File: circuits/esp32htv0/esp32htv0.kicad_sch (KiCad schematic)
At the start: 23 parts, among them J1 Power, SW1 SW_Push, U1 BME280, U2 ESP32-WROOM-32UE, U3 LD1117S33TR_SOT223

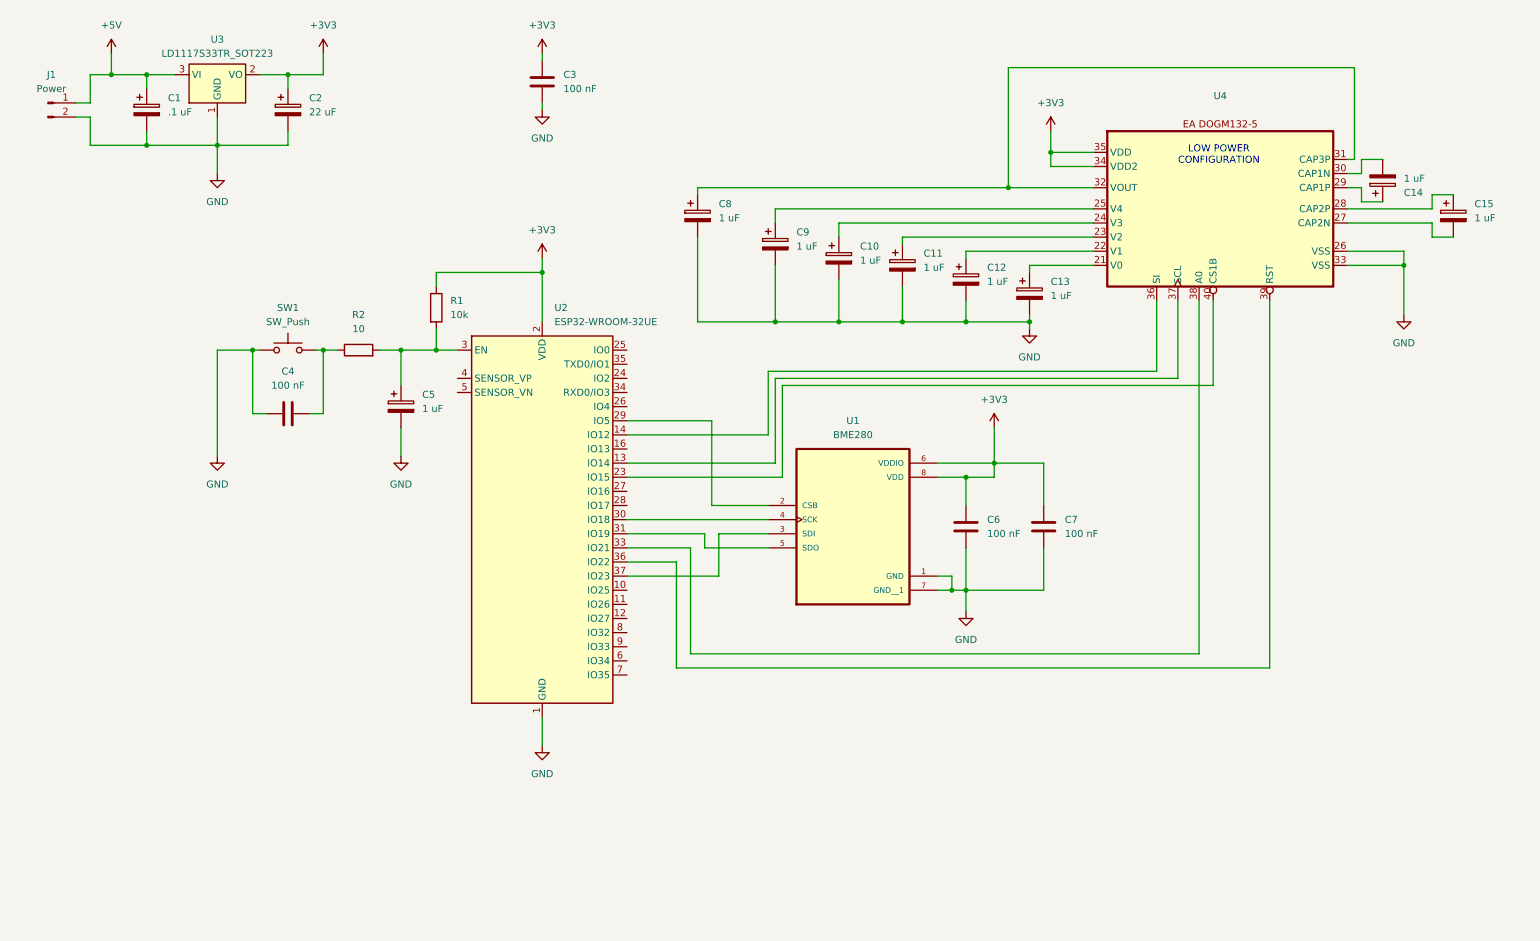
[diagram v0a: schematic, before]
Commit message: Updated ESP32 HTV circuit and a prototype version (esp32htv0) of the same circuit
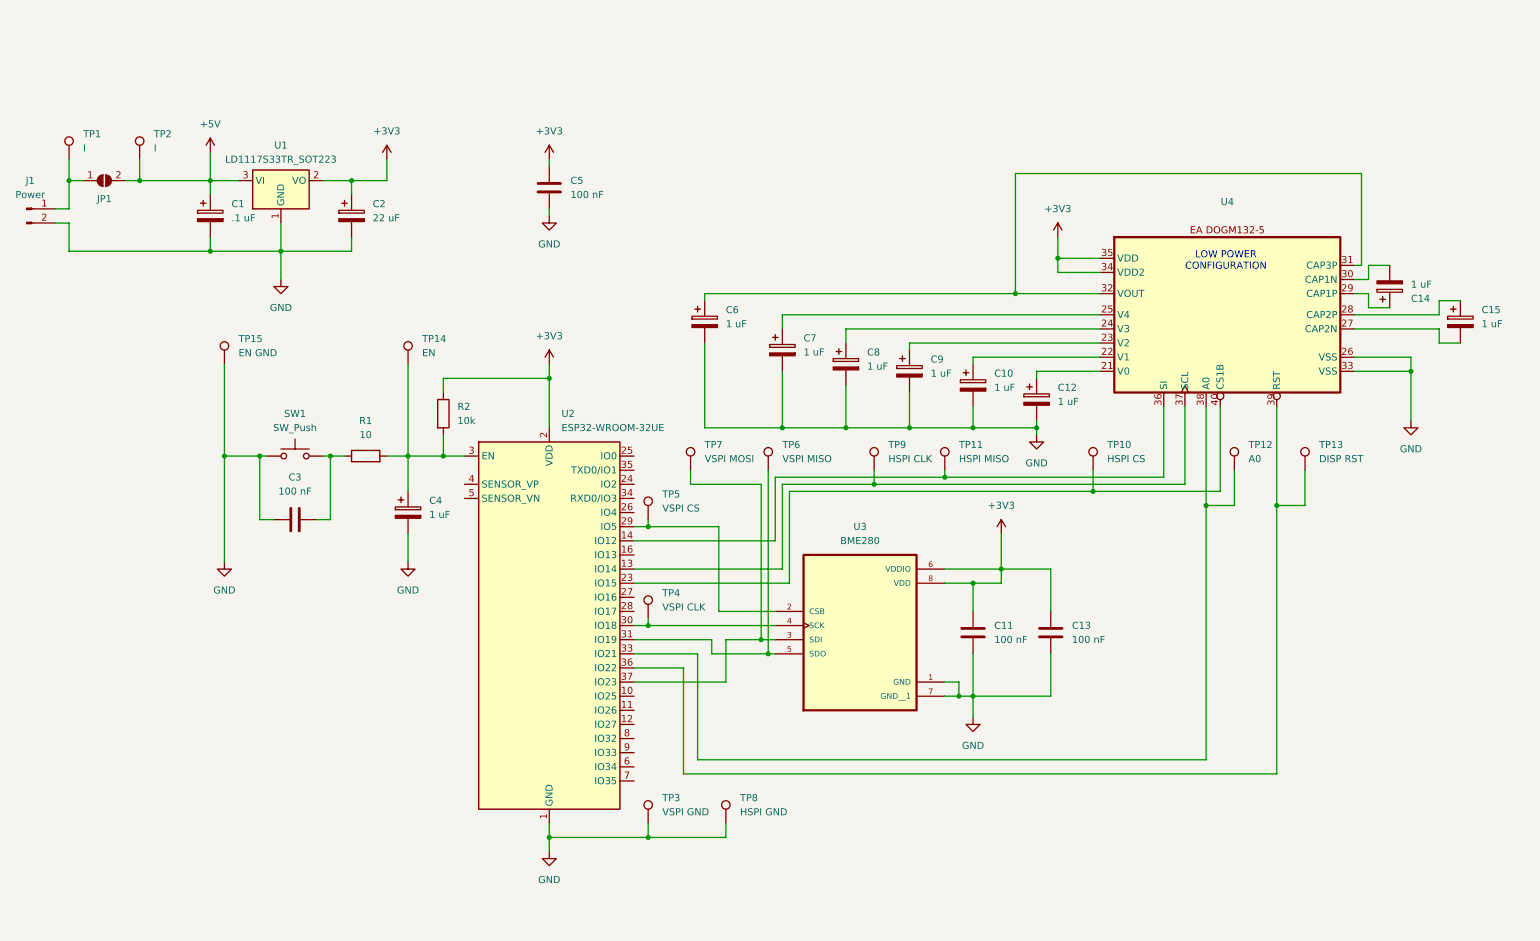
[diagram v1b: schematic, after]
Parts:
- removed C11, C13, C5: 1 uF, Capacitor_SMD:C_1206_3216Metric_Pad1.33x1.80mm_HandSolder, symbol Device:C_Polarized
- removed C4, C6, C7: 100 nF, Capacitor_SMD:C_1206_3216Metric_Pad1.33x1.80mm_HandSolder, symbol Device:C
- removed U1: BME280, gos:PSON65P250X250X100-8N, symbol gos:BME280
- removed U3: LD1117S33TR_SOT223, Package_TO_SOT_SMD:SOT-223-3_TabPin2, symbol Regulator_Linear:LD1117S33TR_SOT223
- added C11, C13, C5: 100 nF, Capacitor_SMD:C_1206_3216Metric_Pad1.33x1.80mm_HandSolder, symbol Device:C
- added C4, C6, C7: 1 uF, Capacitor_SMD:C_1206_3216Metric_Pad1.33x1.80mm_HandSolder, symbol Device:C_Polarized
- added JP1: ID_WP, Jumper:SolderJumper-2_P1.3mm_Open_RoundedPad1.0x1.5mm, symbol Jumper:SolderJumper_2_Open
- added TP1, TP2: I, TestPoint:TestPoint_Loop_D2.50mm_Drill1.0mm, symbol Connector:TestPoint
- added TP10: HSPI CS, TestPoint:TestPoint_Loop_D2.50mm_Drill1.0mm, symbol Connector:TestPoint
- added TP11: HSPI MISO, TestPoint:TestPoint_Loop_D2.50mm_Drill1.0mm, symbol Connector:TestPoint
- added TP12: A0, TestPoint:TestPoint_Loop_D2.50mm_Drill1.0mm, symbol Connector:TestPoint
- added TP13: DISP RST, TestPoint:TestPoint_Loop_D2.50mm_Drill1.0mm, symbol Connector:TestPoint
- added TP14: EN, TestPoint:TestPoint_Loop_D2.50mm_Drill1.0mm, symbol Connector:TestPoint
- added TP15: EN GND, TestPoint:TestPoint_Loop_D2.50mm_Drill1.0mm, symbol Connector:TestPoint
- added TP3: VSPI GND, TestPoint:TestPoint_Loop_D2.50mm_Drill1.0mm, symbol Connector:TestPoint
- added TP4: VSPI CLK, TestPoint:TestPoint_Loop_D2.50mm_Drill1.0mm, symbol Connector:TestPoint
- added TP5: VSPI CS, TestPoint:TestPoint_Loop_D2.50mm_Drill1.0mm, symbol Connector:TestPoint
- added TP6: VSPI MISO, TestPoint:TestPoint_Loop_D2.50mm_Drill1.0mm, symbol Connector:TestPoint
- added TP7: VSPI MOSI, TestPoint:TestPoint_Loop_D2.50mm_Drill1.0mm, symbol Connector:TestPoint
- added TP8: HSPI GND, TestPoint:TestPoint_Loop_D2.50mm_Drill1.0mm, symbol Connector:TestPoint
- added TP9: HSPI CLK, TestPoint:TestPoint_Loop_D2.50mm_Drill1.0mm, symbol Connector:TestPoint
- added U1: LD1117S33TR_SOT223, Package_TO_SOT_SMD:SOT-223-3_TabPin2, symbol Regulator_Linear:LD1117S33TR_SOT223
- added U3: BME280, gos:PSON65P250X250X100-8N, symbol gos:BME280
- J1, SW1: footprint Connector_PinHeader_1.00mm:PinHeader_1x02_P1.00mm_Vertical -> Connector_PinSocket_2.54mm:PinSocket_1x02_P2.54mm_Vertical
- R1: value 10k -> 10
- R2: value 10 -> 10k
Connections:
- net +3V3: now also R2.1, C11.1, C13.1, C5.1, U1.2 (VO), U3.6 (VDDIO), U3.8 (VDD); no longer C3.1, R1.1
- net +5V: now also JP1.2 (B), TP2.1, U1.3 (VI); no longer J1.1 (Pin_1)
- net GND: now also C3.1, C11.2, C13.2, C4.2, C5.2, C6.2, C7.2, TP15.1, TP3.1, TP8.1, U1.1 (GND), U3.1 (GND), U3.7 (GND__1); no longer C3.2
- net at U4.31 (CAP3P), U4.32 (VOUT): now also C6.1; no longer C8.1
- net at R1.2, R2.2, U2.3 (EN): now also C4.1, TP14.1
- net at U4.21 (V0): now also C12.1
- net at U4.22 (V1): now also C10.1; no longer C12.1
- net at U4.23 (V2): now also C9.1
- net at U4.24 (V3): now also C8.1; no longer C10.1
- net at U4.25 (V4): now also C7.1; no longer C9.1
- net at U2.14 (IO12), U4.36 (SI): now also TP11.1
- net at U2.13 (IO14), U4.37 (SCL): now also TP9.1
- net at U2.33 (IO21), U4.38 (A0): now also TP12.1
- net at U2.36 (IO22), U4.39 (RST): now also TP13.1
- net at U2.23 (IO15), U4.40 (CS1B): now also TP10.1
- net at SW1.2: now also C3.2, R1.1; no longer R2.1
- net at U2.29 (IO5): now also TP5.1, U3.2 (CSB)
- net at U2.30 (IO18): now also TP4.1, U3.4 (SCK)
- net at U2.31 (IO19): now also TP6.1, U3.5 (SDO)
- net at U2.37 (IO23): now also TP7.1, U3.3 (SDI)
- new net: J1.1 (Pin_1), JP1.1 (A), TP1.1

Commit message: Updating the ESP32 with HTP concept circuit
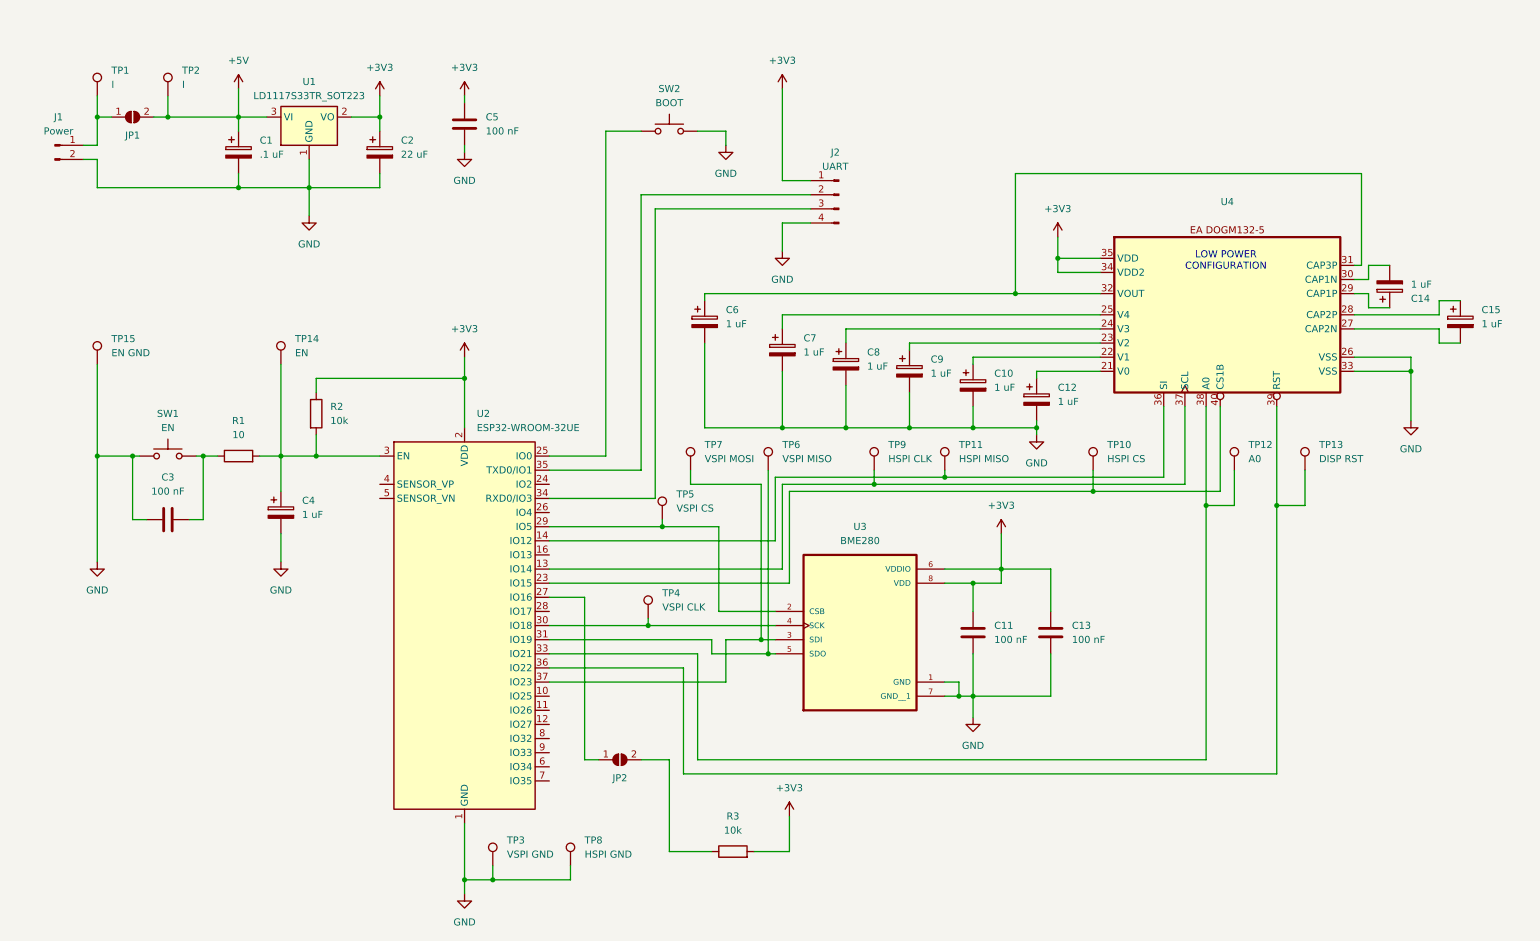
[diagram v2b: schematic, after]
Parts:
- added J2: UART, Connector_PinHeader_2.54mm:PinHeader_1x04_P2.54mm_Vertical, symbol Connector:Conn_01x04_Pin
- added JP2: ID_WP, Jumper:SolderJumper-2_P1.3mm_Open_RoundedPad1.0x1.5mm, symbol Jumper:SolderJumper_2_Open
- added R3: 10k, Resistor_SMD:R_1206_3216Metric_Pad1.30x1.75mm_HandSolder, symbol Device:R
- added SW2: BOOT, Connector_PinSocket_2.54mm:PinSocket_1x02_P2.54mm_Vertical, symbol Switch:SW_Push
- SW1: value SW_Push -> EN
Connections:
- net +3V3: now also J2.1 (Pin_1), R3.2
- net GND: now also J2.4 (Pin_4), SW2.2
- net at U2.25 (IO0): now also SW2.1
- net at U2.27 (IO16): now also JP2.1 (A)
- net at U2.34 (RXD0/IO3): now also J2.3 (Pin_3)
- net at U2.35 (TXD0/IO1): now also J2.2 (Pin_2)
- new net: JP2.2 (B), R3.1
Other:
- moved on the sheet: C1, C2, C3, C4, C5, J1, JP1, R1, R2, SW1, TP1, TP14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

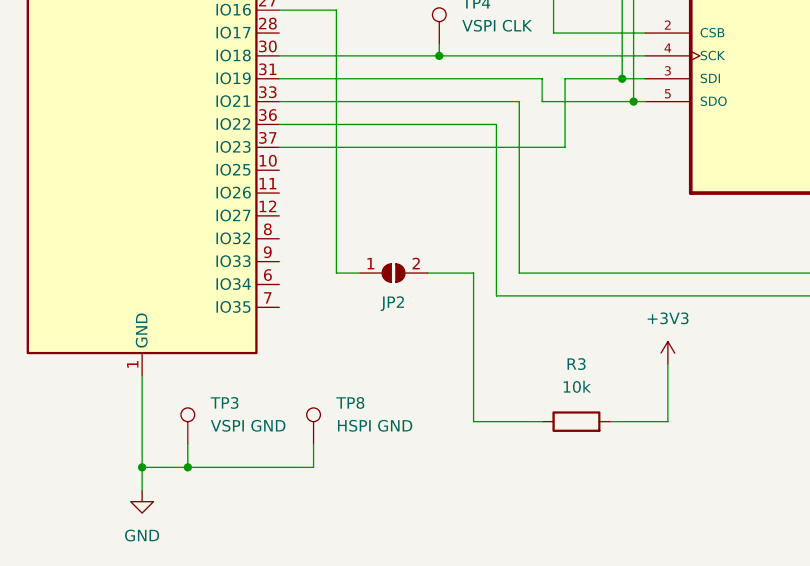
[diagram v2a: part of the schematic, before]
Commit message: Updating the ESP32 HTV circuit and adding some documentation for display options
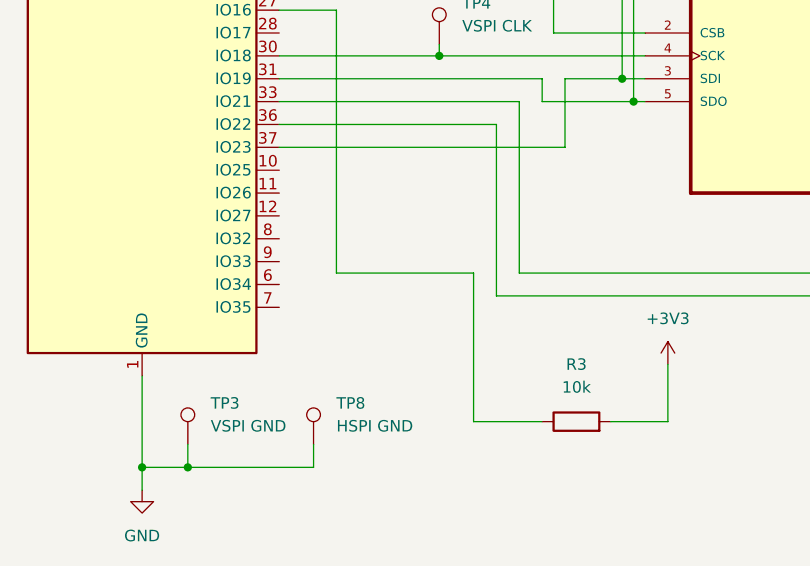
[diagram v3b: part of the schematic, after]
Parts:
- removed JP2: ID_WP, Jumper:SolderJumper-2_P1.3mm_Open_RoundedPad1.0x1.5mm, symbol Jumper:SolderJumper_2_Open
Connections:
- net at R3.1: now also U2.27 (IO16)
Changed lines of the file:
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@@
 	(wire
 		(pts
-			(xy 116.84 148.59) (xy 119.38 148.59)
+			(xy 116.84 148.59) (xy 132.08 148.59)
 		)
 		(stroke
@@
 	(wire
 		(pts
-			(xy 127 148.59) (xy 132.08 148.59)
-		)
-		(stroke
-			(width 0)
-			(type default)
-		)
-	)
-	(wire
-		(pts
 			(xy 270.51 73.66) (xy 274.32 73.66)
 		)
@@
 					(unit 1)
 				)
-			)
-		)
-	)
-	(symbol
-		(lib_id "Jumper:SolderJumper_2_Open")
-		(at 123.19 148.59 0)
-		(unit 1)
-		(exclude_from_sim no)
-		(in_bom yes)
-		(on_board yes)
-		(dnp no)
-		(property "Reference" "JP2"
-			(at 123.19 151.873 0)
-			(effects
-				(font
-					(size 1.27 1.27)
-				)
-			)
-		)
-		(property "Value" "ID_WP"
-			(at 123.19 145.796 0)
-			(effects
-				(font
-					(size 1.27 1.27)
-				)
-				(hide yes)
-			)
-		)
-		(property "Footprint" "Jumper:SolderJumper-2_P1.3mm_Open_RoundedPad1.0x1.5mm"
-			(at 123.19 148.59 0)
-			(effects
-				(font
-					(size 1.27 1.27)
-				)
-				(hide yes)
-			)
-		)
-		(property "Datasheet" "~"
-			(at 123.19 148.59 0)
-			(effects
-				(font
-					(size 1.27 1.27)
-				)
-				(hide yes)
-			)
-		)
-		(property "Description" ""
-			(at 123.19 148.59 0)
-			(effects
-				(font
-					(size 1.27 1.27)
-				)
-				(hide yes)
-			)
-		)
-		(pin "1"
-		)
-		(pin "2"
-		)
-		(instances
-			(project "esp32htv0"
-				(path "/c735b065-5822-4fb3-b1b1-2e3dddcad806"
-					(reference "JP2")
-					(unit 1)
-				)
